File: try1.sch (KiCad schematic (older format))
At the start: 29 parts, among them J10 Archon-connector-modules-Driv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, J11 Archon-connector-modules-Driv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, J2 Archon-connector-modules-Heat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, J21 DB37, J22 DB37, J3 Archon-connector-modules-Driv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, J31 DB9, J4 Archon-connector-modules-LVBi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, J41 CONN_DVI, J5 Archon-connector-modules-ADC, J6 Archon-connector-modules-ADC, J7 Archon-connector-modules-ADC, J8 Archon-connector-modules-ADC, J9 Archon-connector-modules-HVBi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, P1 CONN_02X02

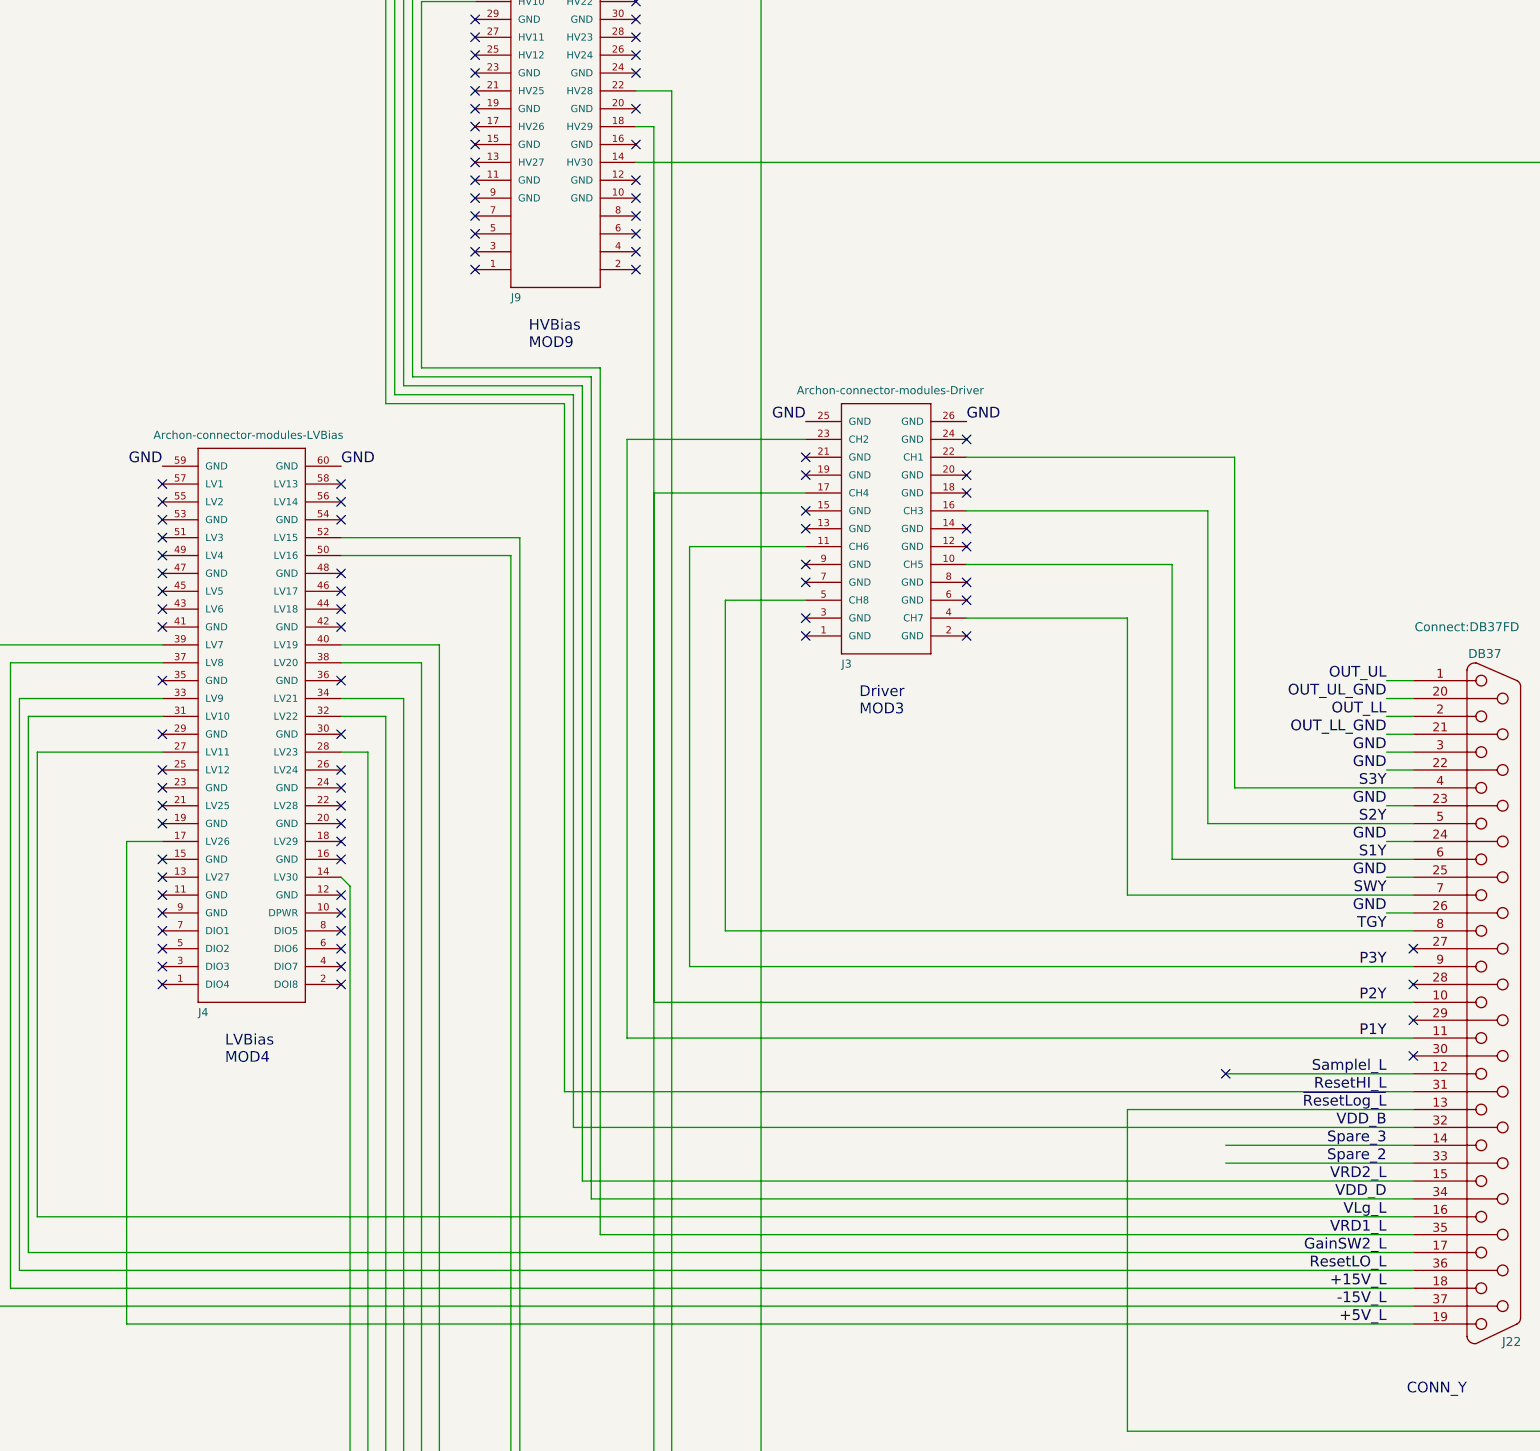
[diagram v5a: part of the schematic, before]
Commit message: Maybe Recovered
Okay, it's not looking too bad.  I reassigned the LVBias and HVBias
high current pins and rerouted some of the LV traces.  It looks like
the rest will work out.
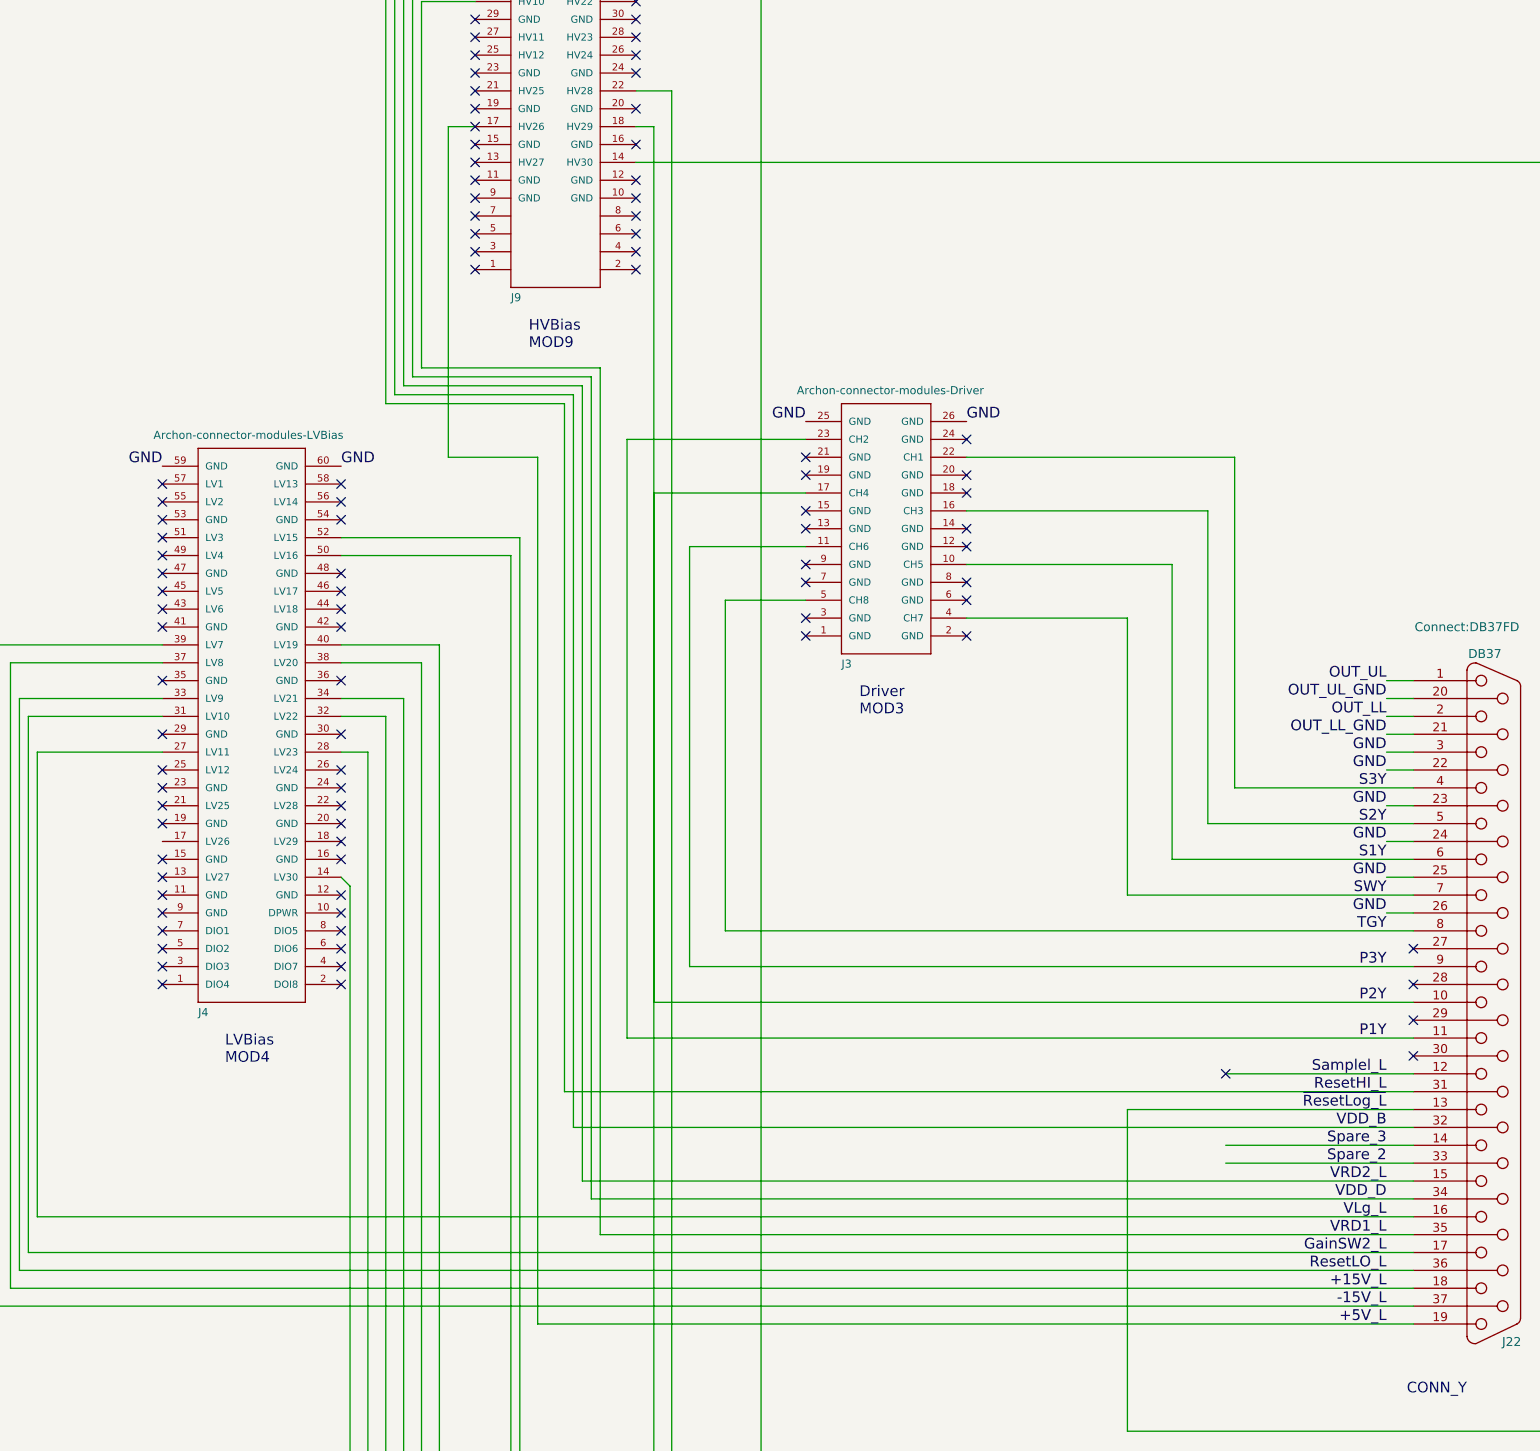
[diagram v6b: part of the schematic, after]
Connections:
- net +5V_L: now also J9.17 (HV26); no longer J4.17 (LV26)
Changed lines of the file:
@@
 	6400 7800 5450 7800
-Wire Wire Line
-	4250 12100 11450 12100
-Wire Wire Line
-	4250 12100 4250 9400
-Wire Wire Line
-	4250 9400 4450 9400
 Wire Wire Line
 	12400 5600 12400 12100
@@
 NoConn ~ 5450 9200
 NoConn ~ 5450 9400
+Wire Wire Line
+	6200 5400 6050 5400
+Wire Wire Line
+	6050 5400 6050 7250
+Wire Wire Line
+	6050 7250 6550 7250
+Wire Wire Line
+	6550 7250 6550 12100
+Wire Wire Line
+	6550 12100 11450 12100
 $EndSCHEMATC

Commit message: WIP Route HVBias, Swap XY HVBias Connections
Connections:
- net ResetHI_L: now also J9.57 (HV1); no longer J9.43 (HV6)
- net ResetHI_R: now also J9.39 (HV7); no longer J9.57 (HV1)
- net VDD_A: now also J9.37 (HV8); no longer J9.55 (HV2)
- net VDD_B: now also J9.55 (HV2); no longer J9.39 (HV7)
- net VDD_C: now also J9.31 (HV10); no longer J9.49 (HV4)
- net VDD_D: now also J9.49 (HV4); no longer J9.33 (HV9)
- net VRD1_L: now also J9.45 (HV5); no longer J9.31 (HV10)
- net VRD1_R: now also J9.27 (HV11); no longer J9.45 (HV5)
- net VRD2_L: now also J9.51 (HV3); no longer J9.37 (HV8)
- net VRD2_R: now also J9.33 (HV9); no longer J9.51 (HV3)

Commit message: WIP: Route HVBias
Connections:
- net +5V_L: now also J9.13 (HV27); no longer J9.17 (HV26)
- net +5V_R: now also J9.17 (HV26); no longer J9.14 (HV30)
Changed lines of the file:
@@
 NoConn ~ 16200 2250
 NoConn ~ 16200 2350
-NoConn ~ 6200 5400
-NoConn ~ 6200 5600
 NoConn ~ 6200 5000
 Text Label 28850 2300 0    60   ~ 0
@@
 	7300 5200 7300 17050
 Wire Wire Line
-	7100 5600 12400 5600
-Wire Wire Line
 	7200 16850 14150 16850
 Wire Wire Line
@@
 	6400 7800 5450 7800
 Wire Wire Line
-	12400 5600 12400 12100
+	12400 5350 12400 12100
 Wire Wire Line
 	7300 5200 7100 5200
@@
 	6200 4550 15900 4550
 Wire Wire Line
-	6200 5400 6050 5400
-Wire Wire Line
-	6050 5400 6050 7250
+	6050 5600 6200 5600
 Wire Wire Line
 	6050 7250 6550 7250
@@
 Wire Wire Line
 	15850 4650 15850 11400
+Wire Wire Line
+	6050 5600 6050 7250
+NoConn ~ 6200 5600
+Wire Wire Line
+	6200 5400 6200 5350
+Wire Wire Line
+	6200 5350 12400 5350
+NoConn ~ 7100 5600
 $EndSCHEMATC
